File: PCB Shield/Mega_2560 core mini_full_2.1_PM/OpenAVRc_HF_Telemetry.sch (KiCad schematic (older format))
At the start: 13 parts, among them P18 Ecolage, P19 Module_TX, P20 TTL/RS232, P3 FTDI, P7 SPIX, U1 74LVC1G3157GV, U2 74LVC1G3157GV, U3 74LVC1G3157GV

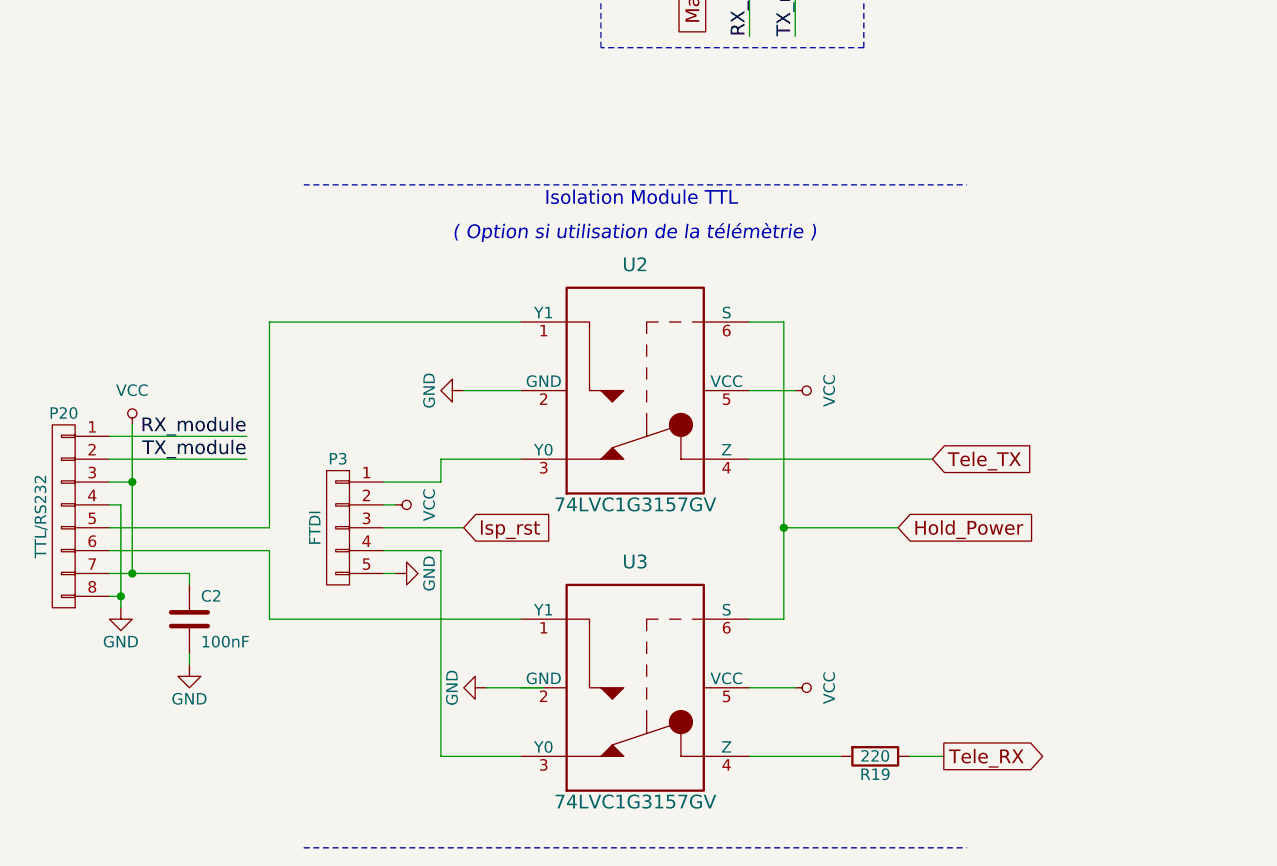
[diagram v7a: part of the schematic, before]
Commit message: Update schematic & pcb files
-add 220ohm on Tele_TX
-update rv1 & rv2 values
-finish pcb .
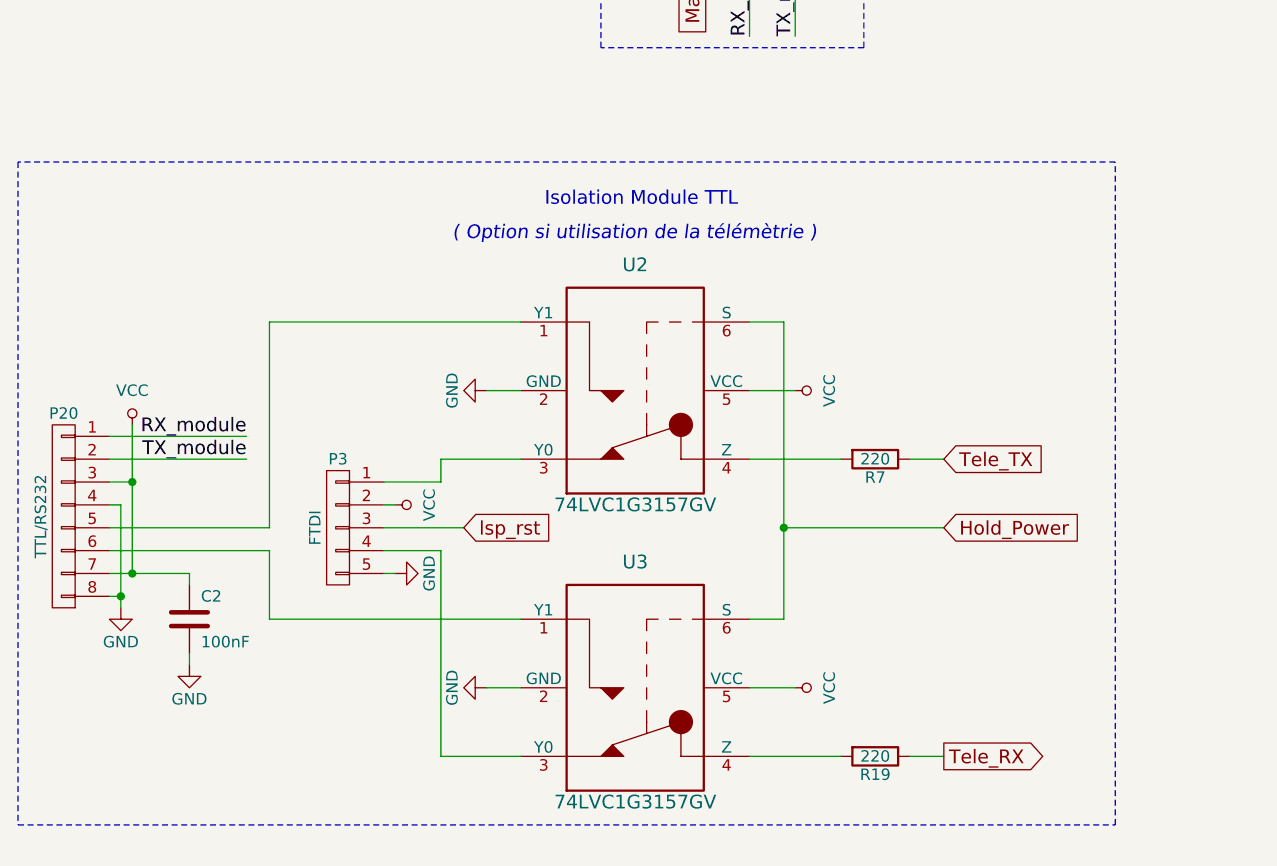
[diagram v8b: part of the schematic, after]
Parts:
- added R7: 220, Resistors_SMD:R_1206, symbol R-RESCUE-Mega_2560_core_mini_full_2.0
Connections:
- net GND: now also U3.2 (GND)
- net Tele_TX: now also R7.1; no longer U2.4 (Z)
- new net: R7.2, U2.4 (Z)
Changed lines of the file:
@@
 Sheet 4 7
 Title "Shield Mega2560 core Full"
-Date "2018-02-25"
+Date "2018-02-28"
 Rev "2.10"
 Comp "© Team OpenAVRc"
@@
 Wire Wire Line
 	9650 4900 9650 5100
-Wire Notes Line
-	1950 6400 4850 6400
-Wire Wire Line
-	3900 4700 4700 4700
 Wire Wire Line
 	4100 1500 4100 2850
@@
 Wire Notes Line
 	6250 3700 10250 3700
-Wire Notes Line
-	1950 3500 4850 3500
 Wire Notes Line
 	4400 800  3250 800
@@
 Text GLabel 4750 6000 2    60   Output ~ 0
 Tele_RX
-Text GLabel 4700 4700 2    60   Input ~ 0
+Text GLabel 4750 4700 2    60   Input ~ 0
 Tele_TX
 Text GLabel 6500 1950 3    60   Input ~ 0
@@
 L GND-RESCUE-Mega_2560_core_mini_full_2.0 #PWR081
 U 1 1 5A9279DC
-P 2650 4400
-F 0 "#PWR081" H 2650 4150 50  0001 C CNN
-F 1 "GND" H 2650 4250 50  0000 C CNN
-F 2 "" H 2650 4400 50  0000 C CNN
-F 3 "" H 2650 4400 50  0000 C CNN
-	1    2650 4400
-	0    1    1    0
-$EndComp
-Wire Wire Line
-	2900 4400 2650 4400
+P 2750 4400
+F 0 "#PWR081" H 2750 4150 50  0001 C CNN
+F 1 "GND" H 2750 4250 50  0000 C CNN
+F 2 "" H 2750 4400 50  0000 C CNN
+F 3 "" H 2750 4400 50  0000 C CNN
+	1    2750 4400
+	0    1    1    0
+$EndComp
+Wire Wire Line
+	2900 4400 2750 4400
 $Comp
 L GND-RESCUE-Mega_2560_core_mini_full_2.0 #PWR082
@@
 	0    1    1    0
 $EndComp
-Wire Wire Line
-	3000 5700 2750 5700
 $Comp
 L CONN_01X05 P3
@@
 	4050 4100 3900 4100
 Wire Wire Line
-	4050 5000 4550 5000
+	4050 5000 4750 5000
 Connection ~ 4050 5000
-Text GLabel 4550 5000 2    60   Input ~ 0
+Text GLabel 4750 5000 2    60   Input ~ 0
 Hold_Power
 Wire Wire Line
@@
 Wire Wire Line
 	2350 4900 2300 4900
+$Comp
+L R-RESCUE-Mega_2560_core_mini_full_2.0 R7
+U 1 1 5A96F891
+P 4450 4700
+F 0 "R7" V 4530 4700 50  0000 C CNN
+F 1 "220" V 4450 4700 50  0000 C CNN
+F 2 "Resistors_SMD:R_1206" V 4380 4700 50  0001 C CNN
+F 3 "" H 4450 4700 50  0000 C CNN
+	1    4450 4700
+	0    1    1    0
+$EndComp
+Wire Wire Line
+	4750 4700 4600 4700
+Wire Wire Line
+	4300 4700 3900 4700
+Wire Notes Line
+	5500 6300 5500 3400
+Wire Notes Line
+	5500 3400 700  3400
+Wire Notes Line
+	700  3400 700  6300
+Wire Notes Line
+	700  6300 5500 6300
+Wire Wire Line
+	2900 5700 2750 5700
 $EndSCHEMATC
